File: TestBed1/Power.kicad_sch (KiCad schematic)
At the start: 0 parts

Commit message: WIP - Parts Assigned
Need footprints, and MCU connections, but WIP
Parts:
- added C5: 4.7u, Capacitor_SMD:C_0805_2012Metric, symbol Device:C
- added C6: 100n, Capacitor_SMD:C_0603_1608Metric, symbol Device:C
- added C7, C9: 4.7u, symbol Device:C
- added L1: 12u, symbol Device:L
- added R3: 100k, symbol Device:R
- added R4: 15.4k, symbol Device:R
- added U4: TPS54308, Package_TO_SOT_SMD:SOT-23-6, symbol Regulator_Switching:TPS54308
- added U5: MIC5365-3.3YC5, Package_TO_SOT_SMD:SOT-353_SC-70-5, symbol Regulator_Linear:MIC5365-3.3YC5
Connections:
- net +5V: now also C7.1, L1.2, R3.1, U5.1 (VIN), U5.3 (EN)
- net CAN_VCC: now also C5.1, U4.3 (VIN), U4.5 (EN)
- new net: C6.2, L1.1, U4.2 (SW)
- new net: R3.2, R4.1, U4.4 (FB)
- new net: C6.1, U4.6 (BOOT)
- new net +3V3: C9.1, U5.5 (VOUT)
- new net GND: C5.2, C7.2, C9.2, R4.2, U4.1 (GND), U5.2 (GND)

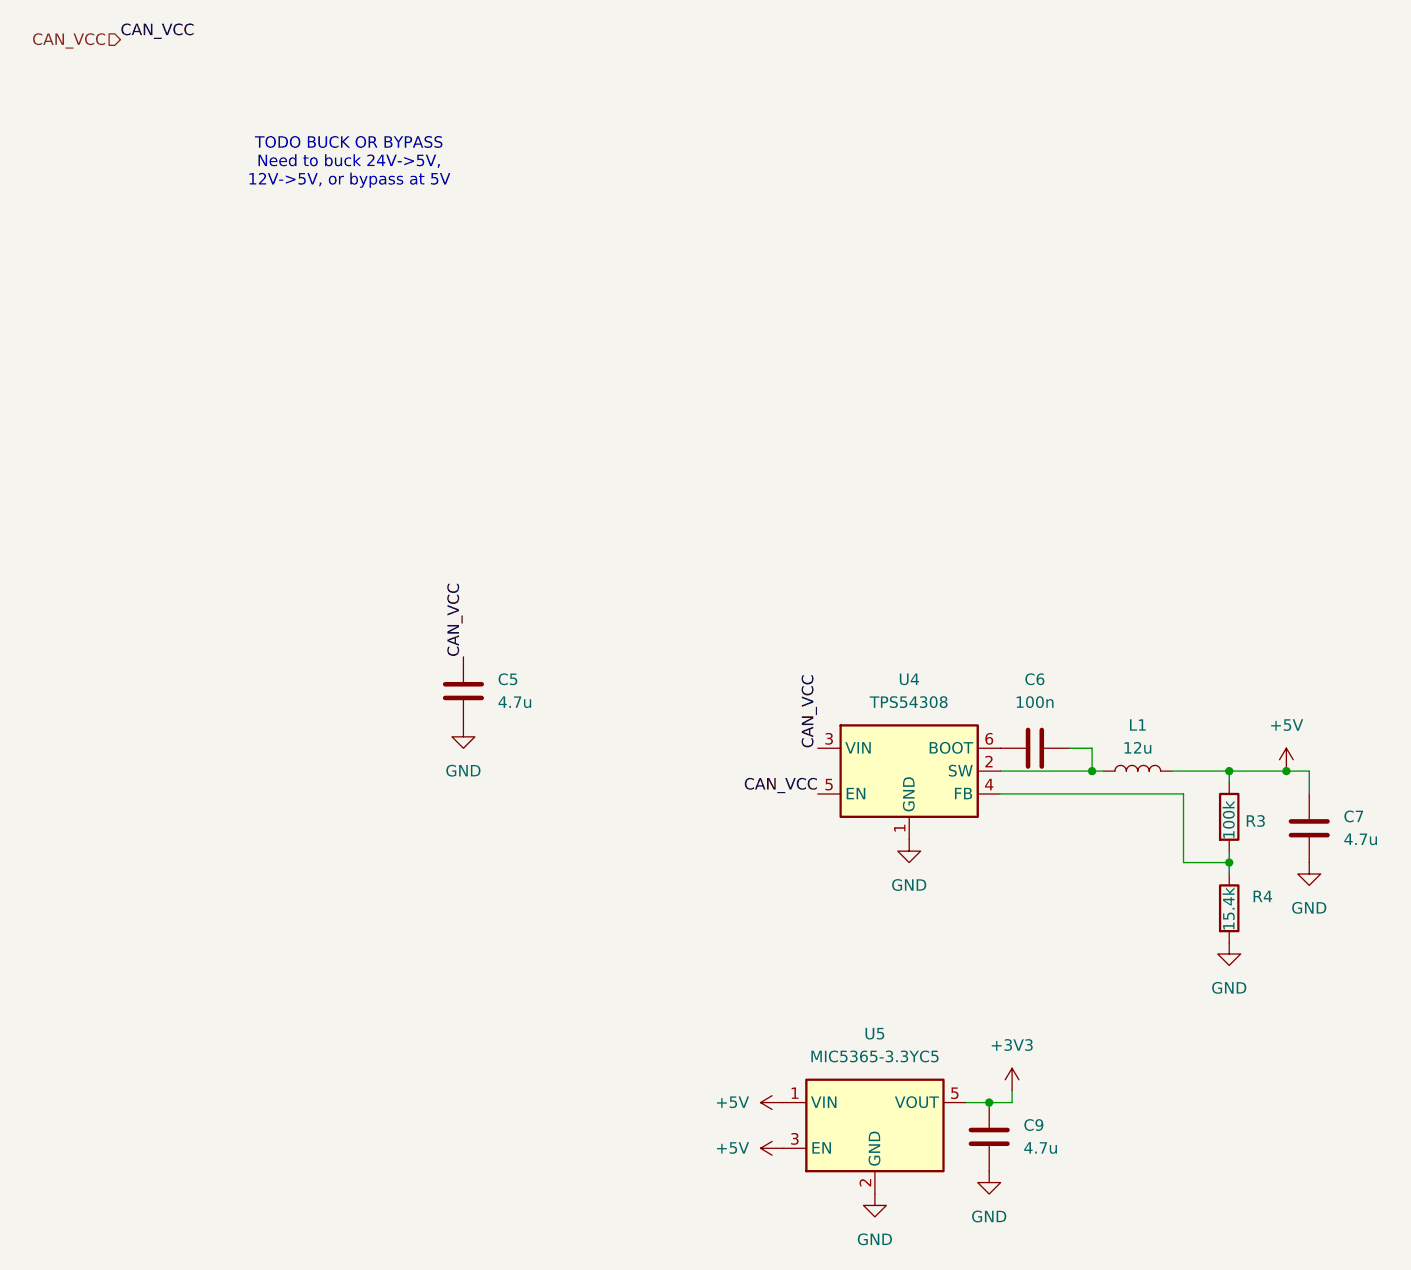
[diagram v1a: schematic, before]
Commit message: Rough Grouping, Passive Footprint Assignment
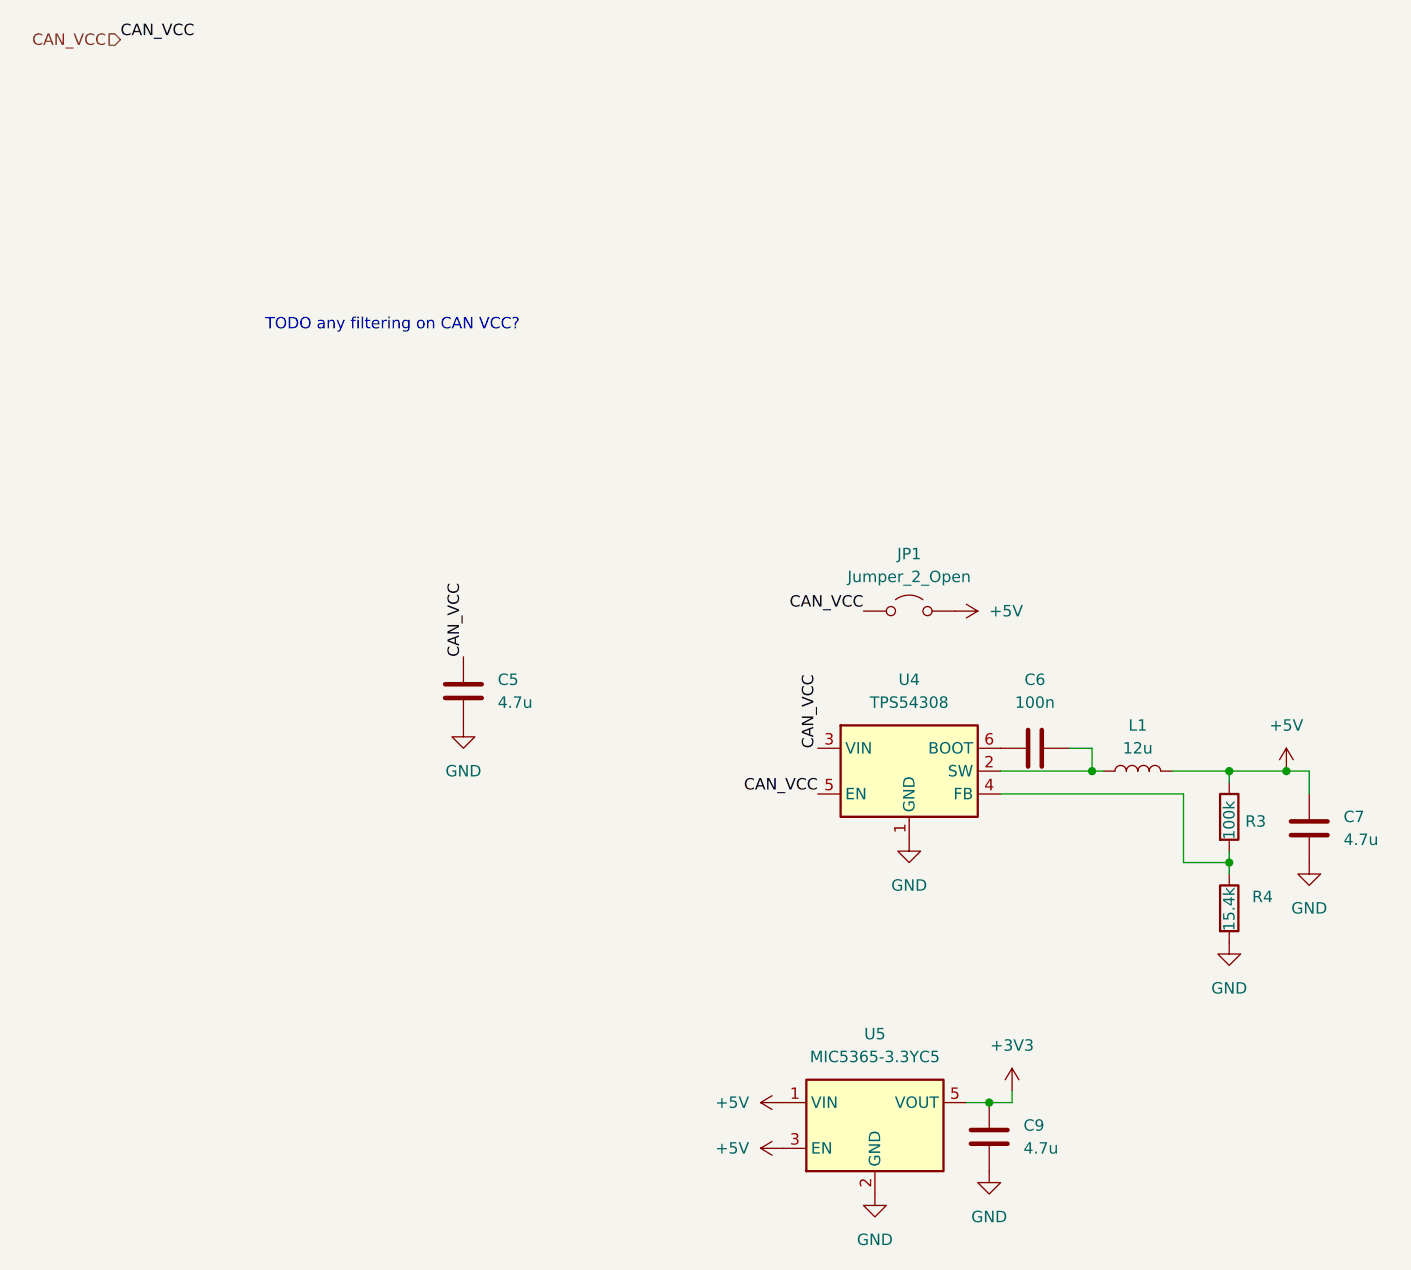
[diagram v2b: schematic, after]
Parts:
- added JP1: Jumper_2_Open, Resistor_SMD:R_0805_2012Metric, symbol Jumper:Jumper_2_Open
- C7, C9: footprint (none) -> Capacitor_SMD:C_0603_1608Metric
- R3, R4: footprint (none) -> Resistor_SMD:R_0402_1005Metric
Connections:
- net +5V: now also JP1.2 (B)
- net CAN_VCC: now also JP1.1 (A)
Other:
- note added: "TODO any filtering on CAN VCC?"
- note removed: "TODO BUCK OR BYPASS Need to buck 24V->5V, 12V->5V, or bypass at 5V"
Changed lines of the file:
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@@
 		)
 	)
-	(text "TODO BUCK OR BYPASS\nNeed to buck 24V->5V, \n12V->5V, or bypass at 5V"
-		(exclude_from_sim no)
-		(at 48.26 28.956 0)
+	(text "TODO any filtering on CAN VCC?"
+		(exclude_from_sim no)
+		(at 53.086 46.99 0)
 		(effects
 			(font
@@
 			)
 			(justify left bottom)
+		)
+	)
+	(label "CAN_VCC"
+		(at 105.41 78.74 180)
+		(effects
+			(font
+				(size 1.27 1.27)
+			)
+			(justify right bottom)
 		)
 	)
@@
 			)
 		)
-		(property "Footprint" ""
+		(property "Footprint" "Capacitor_SMD:C_0603_1608Metric"
 			(at 120.3452 140.97 0)
 			(effects
@@
 	)
 	(symbol
+		(lib_id "Jumper:Jumper_2_Open")
+		(at 110.49 78.74 0)
+		(unit 1)
+		(exclude_from_sim yes)
+		(in_bom yes)
+		(on_board yes)
+		(dnp no)
+		(fields_autoplaced yes)
+		(property "Reference" "JP1"
+			(at 110.49 72.39 0)
+			(effects
+				(font
+					(size 1.27 1.27)
+				)
+			)
+		)
+		(property "Value" "Jumper_2_Open"
+			(at 110.49 74.93 0)
+			(effects
+				(font
+					(size 1.27 1.27)
+				)
+			)
+		)
+		(property "Footprint" "Resistor_SMD:R_0805_2012Metric"
+			(at 110.49 78.74 0)
+			(effects
+				(font
+					(size 1.27 1.27)
+				)
+				(hide yes)
+			)
+		)
+		(property "Datasheet" "~"
+			(at 110.49 78.74 0)
+			(effects
+				(font
+					(size 1.27 1.27)
+				)
+				(hide yes)
+			)
+		)
+		(property "Description" "Jumper, 2-pole, open"
+			(at 110.49 78.74 0)
+			(effects
+				(font
+					(size 1.27 1.27)
+				)
+				(hide yes)
+			)
+		)
+		(pin "2"
+		)
+		(pin "1"
+		)
+		(instances
+			(project ""
+				(path "/1011cb81-baf2-4a82-93dd-e89e67a76dd8/548a5858-c077-4c03-8088-d3b70cd8af24"
+					(reference "JP1")
+					(unit 1)
+				)
+			)
+		)
+	)
+	(symbol
 		(lib_id "Regulator_Linear:MIC5365-3.3YC5")
 		(at 106.68 135.89 0)
@@
 			)
 		)
-		(property "Footprint" ""
+		(property "Footprint" "Resistor_SMD:R_0402_1005Metric"
 			(at 144.272 101.6 90)
 			(effects
@@
 			)
 		)
-		(property "Footprint" ""
+		(property "Footprint" "Resistor_SMD:R_0402_1005Metric"
 			(at 144.272 111.76 90)
 			(effects
@@
 	(symbol
 		(lib_id "power:+5V")
+		(at 115.57 78.74 270)
+		(unit 1)
+		(exclude_from_sim no)
+		(in_bom yes)
+		(on_board yes)
+		(dnp no)
+		(fields_autoplaced yes)
+		(property "Reference" "#PWR051"
+			(at 111.76 78.74 0)
+			(effects
+				(font
+					(size 1.27 1.27)
+				)
+				(hide yes)
+			)
+		)
+		(property "Value" "+5V"
+			(at 119.38 78.7399 90)
+			(effects
+				(font
+					(size 1.27 1.27)
+				)
+				(justify left)
+			)
+		)
+		(property "Footprint" ""
+			(at 115.57 78.74 0)
+			(effects
+				(font
+					(size 1.27 1.27)
+				)
+				(hide yes)
+			)
+		)
+		(property "Datasheet" ""
+			(at 115.57 78.74 0)
+			(effects
+				(font
+					(size 1.27 1.27)
+				)
+				(hide yes)
+			)
+		)
+		(property "Description" "Power symbol creates a global label with name \"+5V\""
+			(at 115.57 78.74 0)
+			(effects
+				(font
+					(size 1.27 1.27)
+				)
+				(hide yes)
+			)
+		)
+		(pin "1"
+		)
+		(instances
+			(project "TestBed1"
+				(path "/1011cb81-baf2-4a82-93dd-e89e67a76dd8/548a5858-c077-4c03-8088-d3b70cd8af24"
+					(reference "#PWR051")
+					(unit 1)
+				)
+			)
+		)
+	)
+	(symbol
+		(lib_id "power:+5V")
 		(at 96.52 133.35 90)
 		(unit 1)
@@
 			)
 		)
-		(property "Footprint" ""
+		(property "Footprint" "Capacitor_SMD:C_0603_1608Metric"
 			(at 155.9052 106.68 0)
 			(effects

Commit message: Schematic Assignment, board assignemtn and rough placement
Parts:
- L1: footprint (none) -> Inductor_SMD:L_1812_4532Metric
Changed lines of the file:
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@@
 	(label "CAN_VCC"
 		(at 100.33 99.06 180)
+		(fields_autoplaced yes)
 		(effects
 			(font
@@
 	(label "CAN_VCC"
 		(at 60.96 83.82 90)
+		(fields_autoplaced yes)
 		(effects
 			(font
@@
 	(label "CAN_VCC"
 		(at 100.33 93.98 90)
+		(fields_autoplaced yes)
 		(effects
 			(font
@@
 	(label "CAN_VCC"
 		(at 105.41 78.74 180)
+		(fields_autoplaced yes)
 		(effects
 			(font
@@
 	(label "CAN_VCC"
 		(at 22.86 15.24 0)
+		(fields_autoplaced yes)
 		(effects
 			(font
@@
 		(shape input)
 		(at 22.86 15.24 180)
+		(fields_autoplaced yes)
 		(effects
 			(font
@@
 			)
 		)
-		(property "Footprint" ""
+		(property "Footprint" "Inductor_SMD:L_1812_4532Metric"
 			(at 135.89 96.52 0)
 			(effects
@@
 			)
 		)
-		(property "Description" "Inductor"
+		(property "Description" "LQH43NH120J03L"
 			(at 135.89 96.52 0)
 			(effects
